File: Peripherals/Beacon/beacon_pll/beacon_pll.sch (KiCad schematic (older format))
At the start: 52 parts, among them J1 Conn_01x12, J4 Conn_Coaxial, U1 LM1117-3.3, U2 TXB0104D, U3 ADF4360-8, U4 QPA4463ASR, X1 ASEMB-10.000MHz

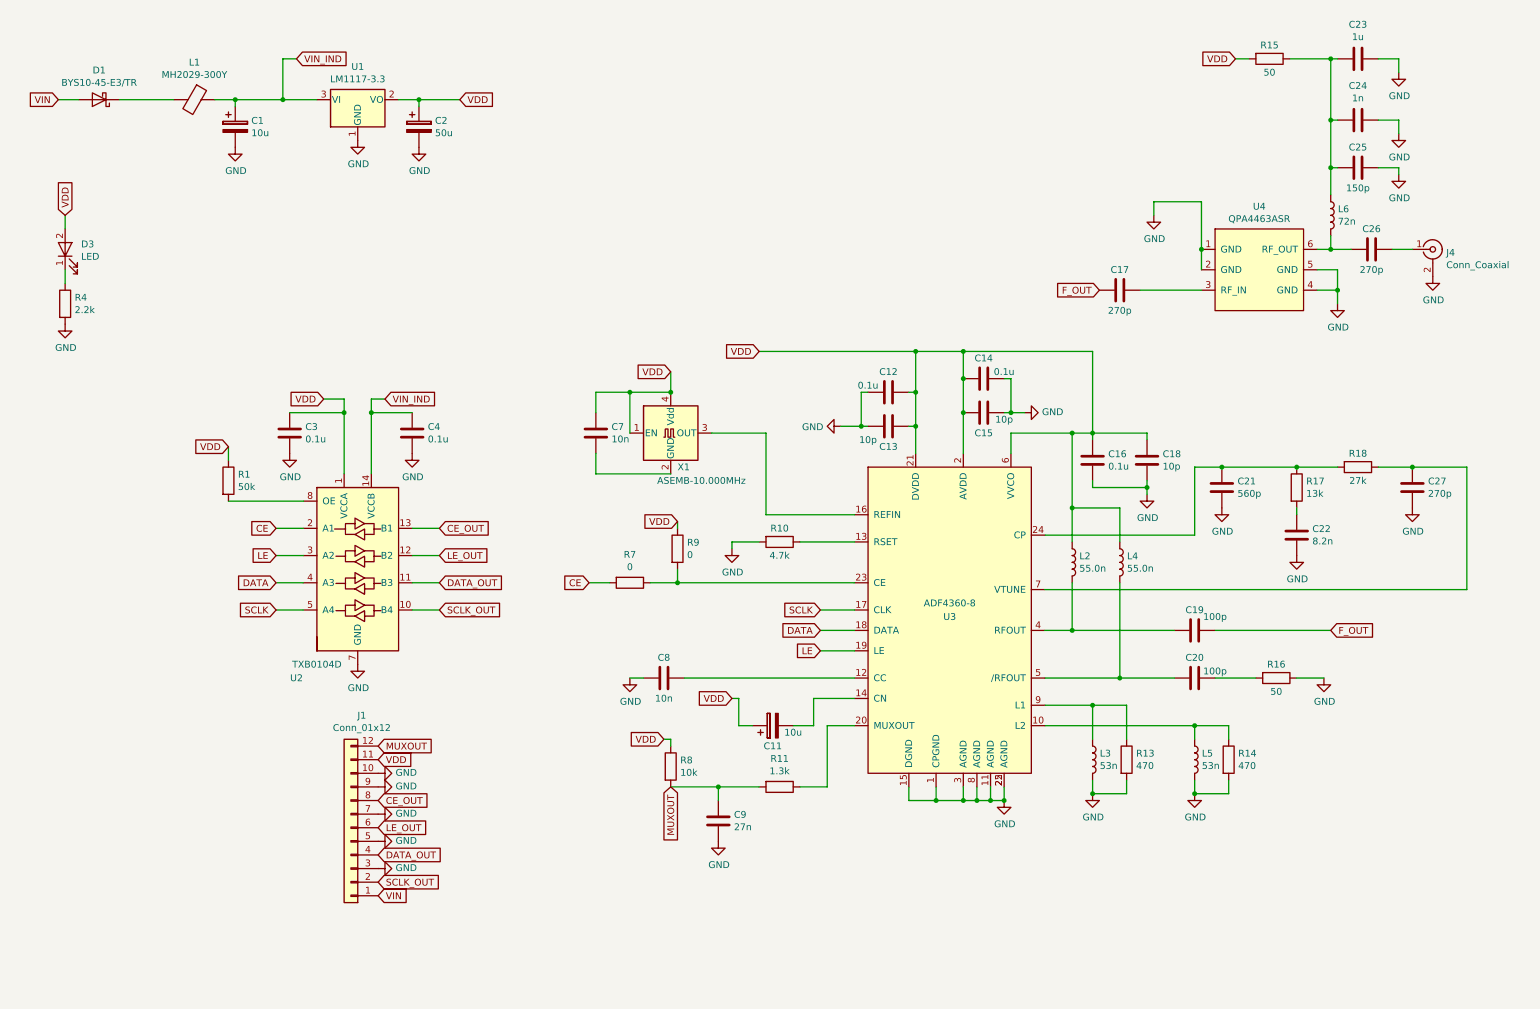
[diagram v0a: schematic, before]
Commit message: Added PDF outputs and cleaned up schematic
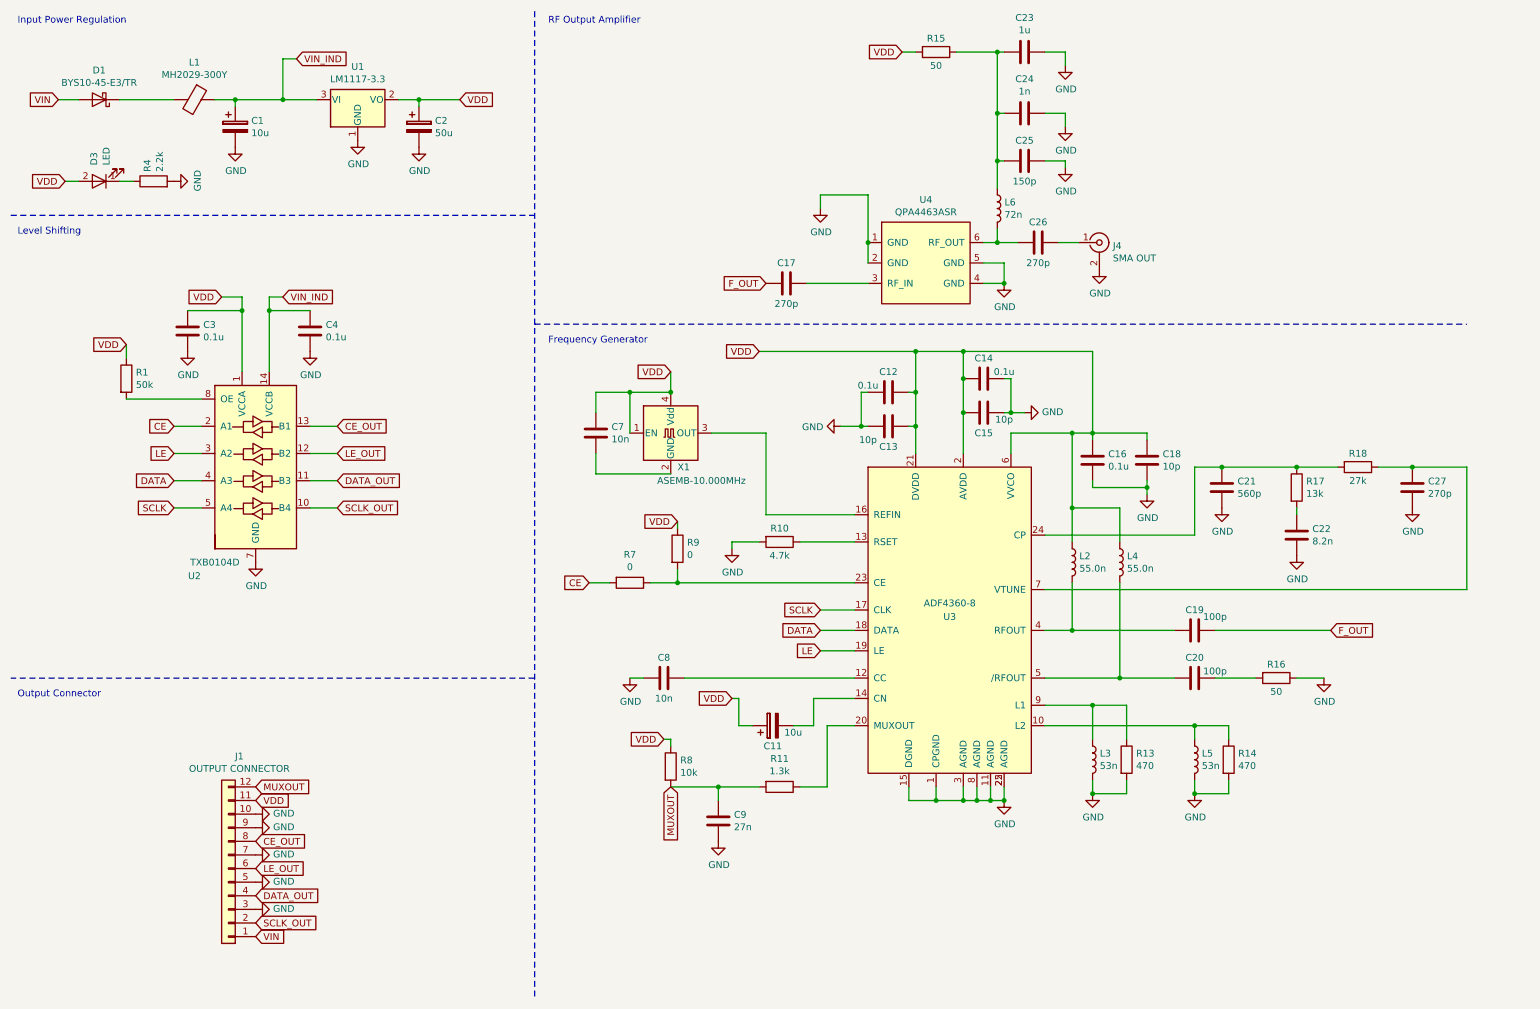
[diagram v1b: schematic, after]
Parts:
- J1: value Conn_01x12 -> OUTPUT CONNECTOR
- J4: value Conn_Coaxial -> SMA OUT
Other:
- note added: "Frequency Generator"
- note added: "Input Power Regulation"
- note added: "Level Shifting"
- note added: "Output Connector"
- note added: "RF Output Amplifier"
- moved on the sheet: C17, C23, C24, C25, C26, C3, C4, D3, J1, J4, L6, R1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
